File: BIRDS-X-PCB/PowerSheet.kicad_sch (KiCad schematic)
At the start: 8 parts, among them Q201 SI1470DH, Q202 SI1470DH, U201 LTC4361-2, U202 LTC4361-2

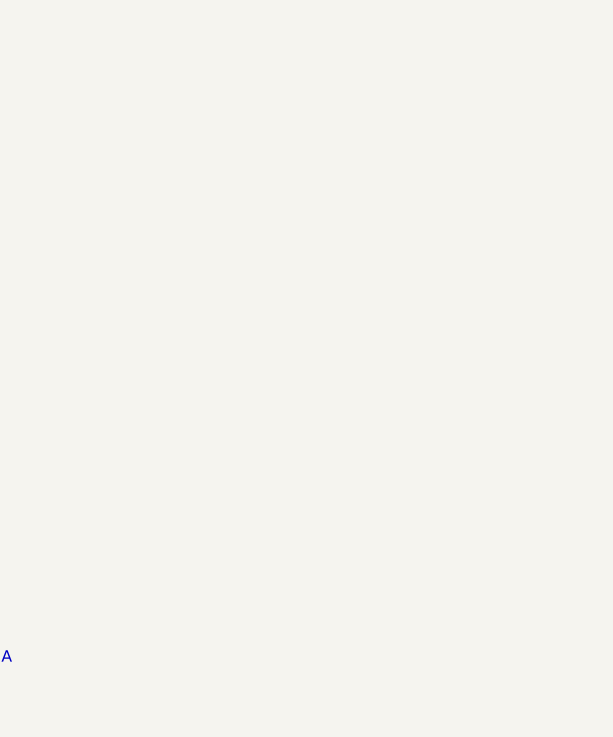
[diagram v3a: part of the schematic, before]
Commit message: Completed MCU & Experiment Circuit
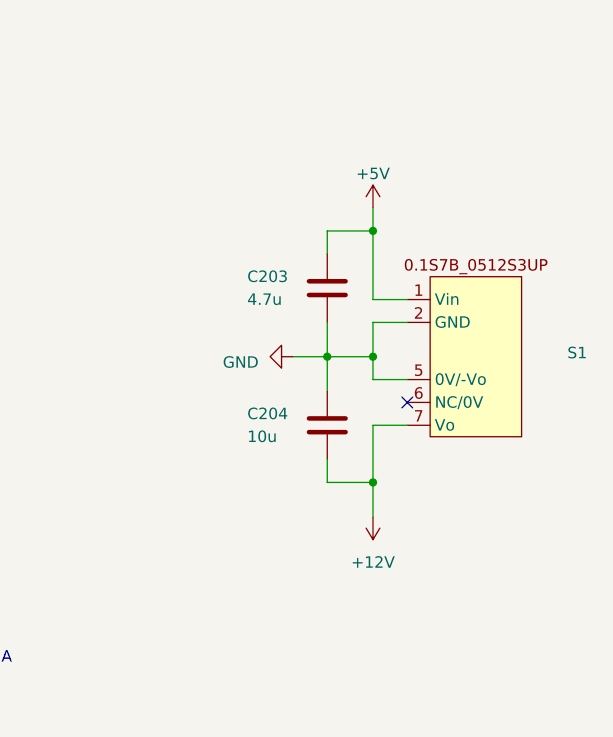
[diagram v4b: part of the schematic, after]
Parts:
- added C203: 4.7u, Capacitor_SMD:C_1206_3216Metric_Pad1.33x1.80mm_HandSolder, symbol Device:C
- added C204: 10u, Capacitor_SMD:C_1206_3216Metric_Pad1.33x1.80mm_HandSolder, symbol Device:C
- added S1: ~, symbol BIRDS-X_Symbols_Lib:1S7B_3UP
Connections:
- net +5V: now also C203.1, S1.1 (Vin)
- net GND: now also C203.2, C204.1, S1.2 (GND), S1.5 (0V/-Vo)
- new net +12V: C204.2, S1.7 (Vo)
- no-connect marks 2 -> 3
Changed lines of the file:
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@@
   (junction (at 83.82 114.3) (diameter 0) (color 0 0 0 0)
   )
+  (junction (at 184.15 81.28) (diameter 0) (color 0 0 0 0)
+  )
   (junction (at 123.19 114.3) (diameter 0) (color 0 0 0 0)
   )
   (junction (at 121.92 41.91) (diameter 0) (color 0 0 0 0)
   )
+  (junction (at 189.23 95.25) (diameter 0) (color 0 0 0 0)
+  )
+  (junction (at 189.23 81.28) (diameter 0) (color 0 0 0 0)
+  )
   (junction (at 68.58 41.91) (diameter 0) (color 0 0 0 0)
   )
+  (junction (at 189.23 67.31) (diameter 0) (color 0 0 0 0)
+  )
   (junction (at 69.85 114.3) (diameter 0) (color 0 0 0 0)
   )
@@
   (junction (at 82.55 41.91) (diameter 0) (color 0 0 0 0)
   )
+  (no_connect (at 193.04 86.36))
   (no_connect (at 105.41 68.58))
   (no_connect (at 106.68 140.97))
+  (wire (pts (xy 189.23 67.31) (xy 189.23 74.93))
+    (stroke (width 0) (type default))
+  )
   (wire (pts (xy 69.85 123.19) (xy 69.85 138.43))
     (stroke (width 0) (type default))
   )
+  (wire (pts (xy 184.15 81.28) (xy 184.15 85.09))
+    (stroke (width 0) (type default))
+  )
   (wire (pts (xy 113.03 114.3) (xy 113.03 135.89))
     (stroke (width 0) (type default))
@@
     (stroke (width 0) (type default))
   )
+  (wire (pts (xy 189.23 83.82) (xy 189.23 81.28))
+    (stroke (width 0) (type default))
+  )
   (wire (pts (xy 83.82 114.3) (xy 83.82 135.89))
     (stroke (width 0) (type default))
@@
     (stroke (width 0) (type default))
   )
+  (wire (pts (xy 184.15 69.85) (xy 184.15 67.31))
+    (stroke (width 0) (type default))
+  )
   (wire (pts (xy 69.85 123.19) (xy 100.33 123.19))
     (stroke (width 0) (type default))
@@
     (stroke (width 0) (type default))
   )
+  (wire (pts (xy 193.04 83.82) (xy 189.23 83.82))
+    (stroke (width 0) (type default))
+  )
+  (wire (pts (xy 180.34 81.28) (xy 184.15 81.28))
+    (stroke (width 0) (type default))
+  )
   (wire (pts (xy 29.21 24.13) (xy 31.75 24.13))
     (stroke (width 0) (type default))
@@
     (stroke (width 0) (type default))
   )
+  (wire (pts (xy 184.15 95.25) (xy 189.23 95.25))
+    (stroke (width 0) (type default))
+  )
+  (wire (pts (xy 189.23 64.77) (xy 189.23 67.31))
+    (stroke (width 0) (type default))
+  )
+  (wire (pts (xy 184.15 81.28) (xy 189.23 81.28))
+    (stroke (width 0) (type default))
+  )
   (wire (pts (xy 80.01 41.91) (xy 82.55 41.91))
     (stroke (width 0) (type default))
@@
     (stroke (width 0) (type default))
   )
+  (wire (pts (xy 189.23 77.47) (xy 189.23 81.28))
+    (stroke (width 0) (type default))
+  )
   (wire (pts (xy 82.55 41.91) (xy 82.55 63.5))
     (stroke (width 0) (type default))
@@
     (stroke (width 0) (type default))
   )
+  (wire (pts (xy 193.04 88.9) (xy 189.23 88.9))
+    (stroke (width 0) (type default))
+  )
   (wire (pts (xy 68.58 41.91) (xy 68.58 50.8))
     (stroke (width 0) (type default))
@@
     (stroke (width 0) (type default))
   )
+  (wire (pts (xy 184.15 77.47) (xy 184.15 81.28))
+    (stroke (width 0) (type default))
+  )
   (wire (pts (xy 111.76 63.5) (xy 105.41 63.5))
     (stroke (width 0) (type default))
   )
+  (wire (pts (xy 189.23 95.25) (xy 189.23 99.06))
+    (stroke (width 0) (type default))
+  )
   (wire (pts (xy 83.82 135.89) (xy 88.9 135.89))
     (stroke (width 0) (type default))
   )
+  (wire (pts (xy 189.23 74.93) (xy 193.04 74.93))
+    (stroke (width 0) (type default))
+  )
   (wire (pts (xy 96.52 77.47) (xy 96.52 81.28))
     (stroke (width 0) (type default))
   )
+  (wire (pts (xy 193.04 77.47) (xy 189.23 77.47))
+    (stroke (width 0) (type default))
+  )
   (wire (pts (xy 96.52 121.92) (xy 96.52 125.73))
     (stroke (width 0) (type default))
   )
+  (wire (pts (xy 184.15 67.31) (xy 189.23 67.31))
+    (stroke (width 0) (type default))
+  )
   (wire (pts (xy 121.92 41.91) (xy 121.92 45.72))
     (stroke (width 0) (type default))
@@
     (stroke (width 0) (type default))
   )
+  (wire (pts (xy 184.15 92.71) (xy 184.15 95.25))
+    (stroke (width 0) (type default))
+  )
   (wire (pts (xy 123.19 125.73) (xy 123.19 132.08))
     (stroke (width 0) (type default))
@@
   )
   (wire (pts (xy 82.55 63.5) (xy 87.63 63.5))
+    (stroke (width 0) (type default))
+  )
+  (wire (pts (xy 189.23 88.9) (xy 189.23 95.25))
     (stroke (width 0) (type default))
   )
@@
         (path "/c2796b15-795a-4d6e-ad4b-0ba87ded4bc9/f0b1214b-f453-423f-b2cf-f5d10e08eafe"
           (reference "#PWR0206") (unit 1)
+        )
+      )
+    )
+  )
+  (symbol (lib_id "power:+12V") (at 189.23 99.06 180) (unit 1)
+    (in_bom yes) (on_board yes) (dnp no) (fields_autoplaced)
+    (property "Reference" "#PWR015" (at 189.23 95.25 0)
+      (effects (font (size 1.27 1.27)) hide)
+    )
+    (property "Value" "+12V" (at 189.23 104.14 0)
+      (effects (font (size 1.27 1.27)))
+    )
+    (property "Footprint" "" (at 189.23 99.06 0)
+      (effects (font (size 1.27 1.27)) hide)
+    )
+    (property "Datasheet" "" (at 189.23 99.06 0)
+      (effects (font (size 1.27 1.27)) hide)
+    )
+    (pin "1")
+    (instances
+      (project "BIRDS-X-PCB"
+        (path "/c2796b15-795a-4d6e-ad4b-0ba87ded4bc9/f0b1214b-f453-423f-b2cf-f5d10e08eafe"
+          (reference "#PWR015") (unit 1)
         )
       )
@@
     )
   )
+  (symbol (lib_id "Device:C") (at 184.15 73.66 0) (unit 1)
+    (in_bom yes) (on_board yes) (dnp no)
+    (property "Reference" "C203" (at 175.26 72.39 0)
+      (effects (font (size 1.27 1.27)) (justify left))
+    )
+    (property "Value" "4.7u" (at 175.26 74.93 0)
+      (effects (font (size 1.27 1.27)) (justify left))
+    )
+    (property "Footprint" "Capacitor_SMD:C_1206_3216Metric_Pad1.33x1.80mm_HandSolder" (at 185.1152 77.47 0)
+      (effects (font (size 1.27 1.27)) hide)
+    )
+    (property "Datasheet" "~" (at 184.15 73.66 0)
+      (effects (font (size 1.27 1.27)) hide)
+    )
+    (pin "1")
+    (pin "2")
+    (instances
+      (project "BIRDS-X-PCB"
+        (path "/c2796b15-795a-4d6e-ad4b-0ba87ded4bc9/f0b1214b-f453-423f-b2cf-f5d10e08eafe"
+          (reference "C203") (unit 1)
+        )
+      )
+    )
+  )
   (symbol (lib_id "power:GND") (at 123.19 132.08 0) (unit 1)
     (in_bom yes) (on_board yes) (dnp no) (fields_autoplaced)
@@
     )
   )
+  (symbol (lib_id "power:GND") (at 180.34 81.28 270) (unit 1)
+    (in_bom yes) (on_board yes) (dnp no) (fields_autoplaced)
+    (property "Reference" "#PWR08" (at 173.99 81.28 0)
+      (effects (font (size 1.27 1.27)) hide)
+    )
+    (property "Value" "GND" (at 176.53 81.915 90)
+      (effects (font (size 1.27 1.27)) (justify right))
+    )
+    (property "Footprint" "" (at 180.34 81.28 0)
+      (effects (font (size 1.27 1.27)) hide)
+    )
+    (property "Datasheet" "" (at 180.34 81.28 0)
+      (effects (font (size 1.27 1.27)) hide)
+    )
+    (pin "1")
+    (instances
+      (project "BIRDS-X-PCB"
+        (path "/c2796b15-795a-4d6e-ad4b-0ba87ded4bc9"
+          (reference "#PWR08") (unit 1)
+        )
+        (path "/c2796b15-795a-4d6e-ad4b-0ba87ded4bc9/f0b1214b-f453-423f-b2cf-f5d10e08eafe"
+          (reference "#PWR010") (unit 1)
+        )
+      )
+    )
+  )
   (symbol (lib_id "Device:R") (at 76.2 41.91 90) (unit 1)
     (in_bom yes) (on_board yes) (dnp no) (fields_autoplaced)
@@
         (path "/c2796b15-795a-4d6e-ad4b-0ba87ded4bc9/f0b1214b-f453-423f-b2cf-f5d10e08eafe"
           (reference "C202") (unit 1)
+        )
+      )
+    )
+  )
+  (symbol (lib_id "Device:C") (at 184.15 88.9 0) (unit 1)
+    (in_bom yes) (on_board yes) (dnp no)
+    (property "Reference" "C204" (at 175.26 87.63 0)
+      (effects (font (size 1.27 1.27)) (justify left))
+    )
+    (property "Value" "10u" (at 175.26 90.17 0)
+      (effects (font (size 1.27 1.27)) (justify left))
+    )
+    (property "Footprint" "Capacitor_SMD:C_1206_3216Metric_Pad1.33x1.80mm_HandSolder" (at 185.1152 92.71 0)
+      (effects (font (size 1.27 1.27)) hide)
+    )
+    (property "Datasheet" "~" (at 184.15 88.9 0)
+      (effects (font (size 1.27 1.27)) hide)
+    )
+    (pin "1")
+    (pin "2")
+    (instances
+      (project "BIRDS-X-PCB"
+        (path "/c2796b15-795a-4d6e-ad4b-0ba87ded4bc9/f0b1214b-f453-423f-b2cf-f5d10e08eafe"
+          (reference "C204") (unit 1)
         )
       )
@@
     )
   )
+  (symbol (lib_id "power:+5V") (at 189.23 64.77 0) (unit 1)
+    (in_bom yes) (on_board yes) (dnp no) (fields_autoplaced)
+    (property "Reference" "#PWR07" (at 189.23 68.58 0)
+      (effects (font (size 1.27 1.27)) hide)
+    )
+    (property "Value" "+5V" (at 189.23 60.96 0)
+      (effects (font (size 1.27 1.27)))
+    )
+    (property "Footprint" "" (at 189.23 64.77 0)
+      (effects (font (size 1.27 1.27)) hide)
+    )
+    (property "Datasheet" "" (at 189.23 64.77 0)
+      (effects (font (size 1.27 1.27)) hide)
+    )
+    (pin "1")
+    (instances
+      (project "BIRDS-X-PCB"
+        (path "/c2796b15-795a-4d6e-ad4b-0ba87ded4bc9/f0b1214b-f453-423f-b2cf-f5d10e08eafe"
+          (reference "#PWR07") (unit 1)
+        )
+      )
+    )
+  )
   (symbol (lib_id "power:GND") (at 96.52 81.28 0) (unit 1)
     (in_bom yes) (on_board yes) (dnp no) (fields_autoplaced)
@@
         )
       )
+    )
+  )
+  (symbol (lib_id "BIRDS-X_Symbols_Lib:1S7B_3UP") (at 200.66 81.28 0) (unit 1)
+    (in_bom yes) (on_board yes) (dnp no) (fields_autoplaced)
+    (property "Reference" "S1" (at 210.82 80.8632 0)
+      (effects (font (size 1.27 1.27)) (justify left))
+    )
+    (property "Value" "~" (at 198.12 81.28 90)
+      (effects (font (size 1.27 1.27)))
+    )
+    (property "Footprint" "" (at 198.12 81.28 90)
+      (effects (font (size 1.27 1.27)) hide)
+    )
+    (property "Datasheet" "" (at 198.12 81.28 90)
+      (effects (font (size 1.27 1.27)) hide)
+    )
+    (pin "1")
+    (pin "2")
+    (pin "5")
+    (pin "6")
+    (pin "7")
+    (instances
+      (project "BIRDS-X-PCB"
+        (path "/c2796b15-795a-4d6e-ad4b-0ba87ded4bc9/f0b1214b-f453-423f-b2cf-f5d10e08eafe"
+          (reference "S1") (unit 1)
+        )
+      )

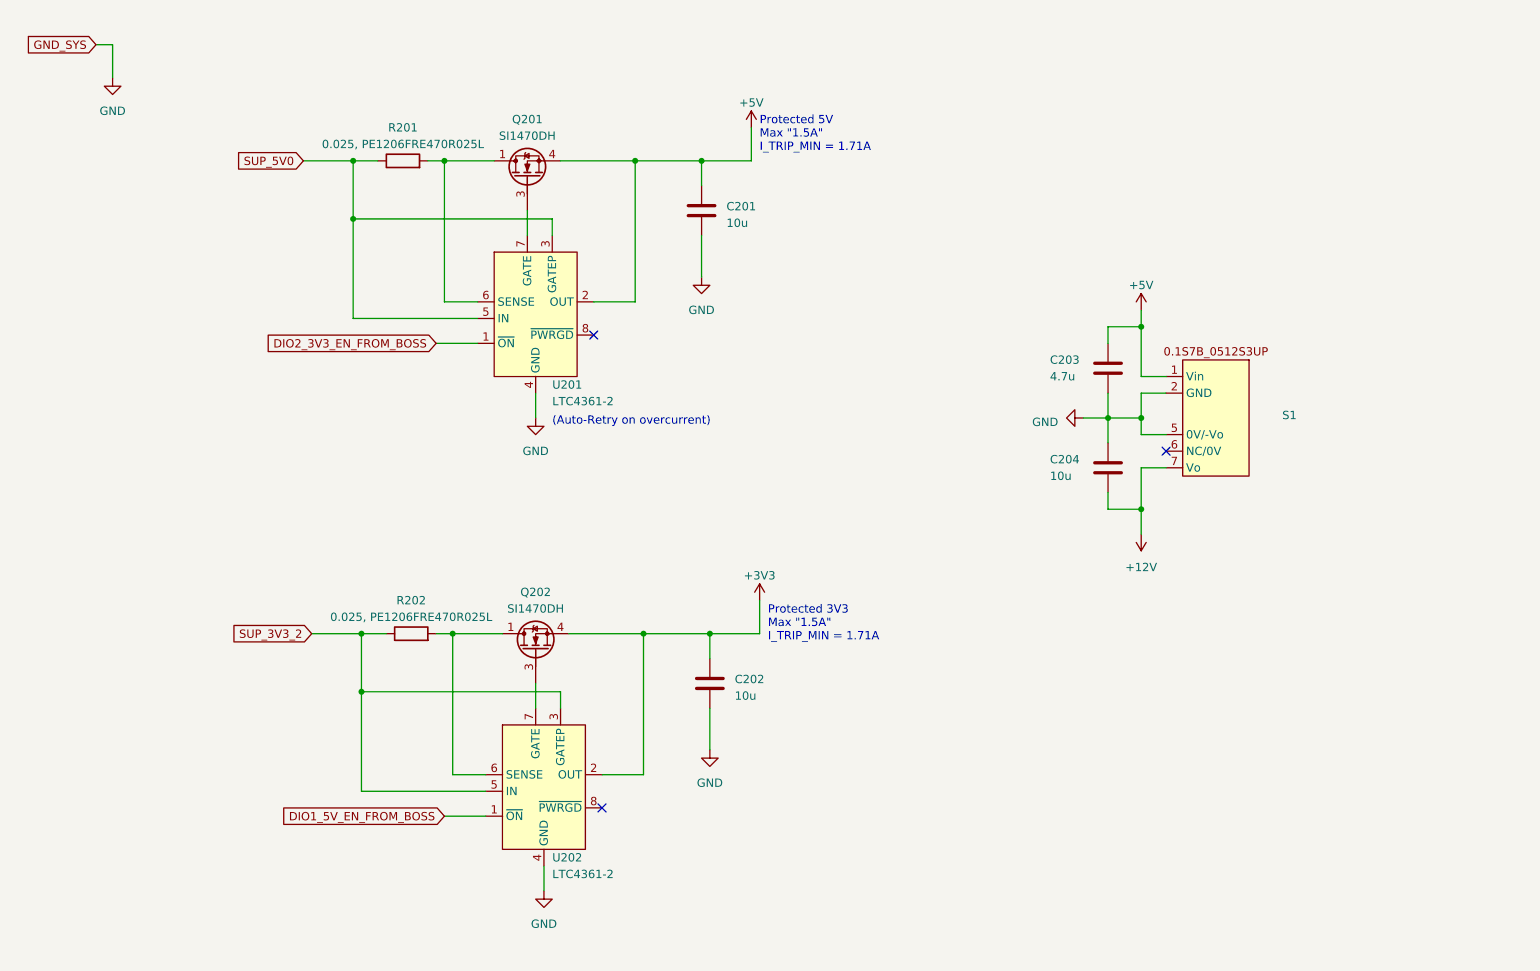
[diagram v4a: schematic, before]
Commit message: Semantic and symbol updates, begin review changes
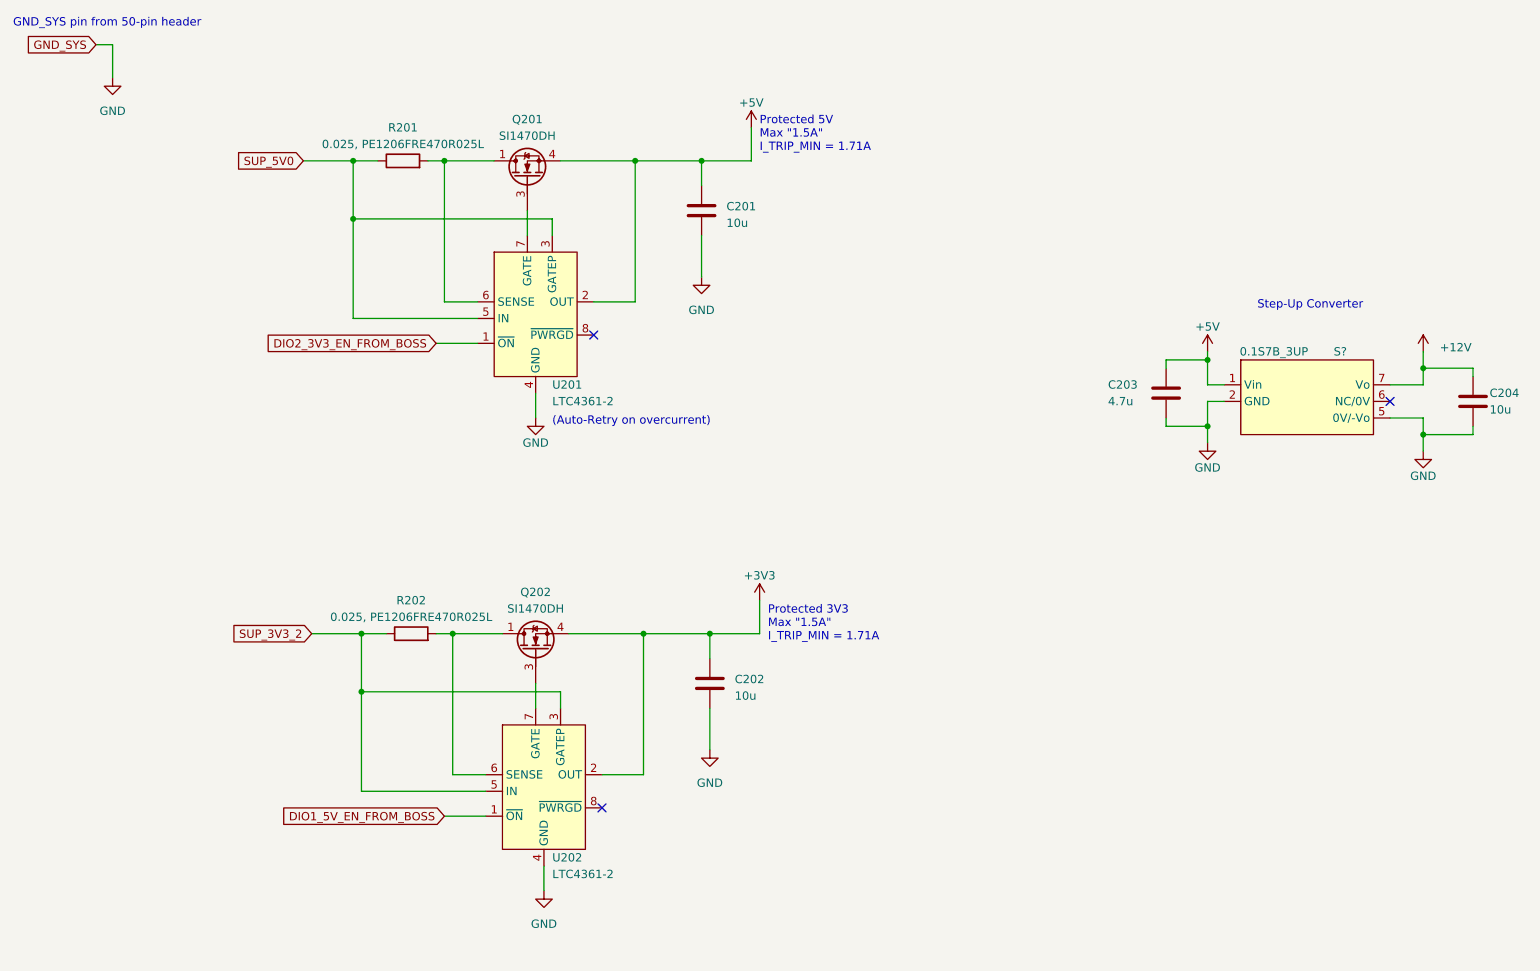
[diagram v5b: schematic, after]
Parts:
- S?: renamed from S1; value ~ -> 0.1S7B_3UP; symbol BIRDS-X_Symbols_Lib:1S7B_3UP -> BIRDS-X_Symbols_Lib:0.1S7B_3UP
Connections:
- net +12V: now also C204.1; no longer C204.2
- net GND: now also C204.2; no longer C204.1
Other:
- note added: "GND_SYS pin from 50-pin header"
- note added: "Step-Up Converter"
- moved on the sheet: C203, C204

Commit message: Add more MCU changes
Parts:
- gave numbers to parts that had none: 1
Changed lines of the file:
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@@
   (symbol (lib_id "BIRDS-X_Symbols_Lib:0.1S7B_3UP") (at 209.55 78.74 0) (unit 1)
     (in_bom yes) (on_board yes) (dnp no)
-    (property "Reference" "S?" (at 219.71 71.12 0)
+    (property "Reference" "S201" (at 219.71 71.12 0)
       (effects (font (size 1.27 1.27)))
     )
@@
       (project "BIRDS-X-PCB"
         (path "/c2796b15-795a-4d6e-ad4b-0ba87ded4bc9/f0b1214b-f453-423f-b2cf-f5d10e08eafe"
-          (reference "S?") (unit 1)
+          (reference "S201") (unit 1)
         )
       )
